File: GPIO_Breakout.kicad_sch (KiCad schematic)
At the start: 3 parts, among them J10 Port C/D breakout, J8 Port A breakout, J9 Port B breakout

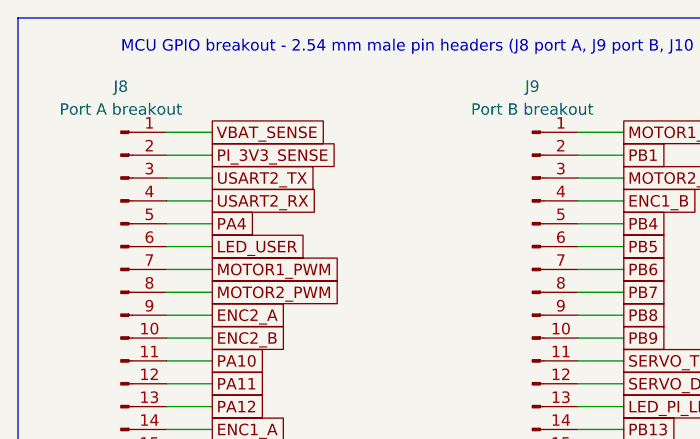
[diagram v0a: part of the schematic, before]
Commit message: Switch AUX ports to top-entry JST XH; drop encoder pull-ups and Pi sense
- J18-J21 (peripheral 5 V ports) are now top-entry JST XH B2B-XH-A:
  cables plug in from above, which suits a flat board you reach into,
  and the footprint drops from 107 to 58 mm2 per port. Use pre-made
  2-pin XH cables, so no crimping.
- Remove the DNP encoder pull-ups R48-R51. If the am-3651 outputs turn
  out to be open-collector, bodge 4.7k from each A/B line to ENCn_5V
  (noted on the Motor Control sheet).
- Remove the Pi-alive sense R44/R45. PA1 is a spare pin again (J8 pin
  2); the Pi's 3V3 on J13 still enables the AUX buck through D15.
- Board: same edits as Update PCB from Schematic (J18-J21 swapped,
  six resistors deleted, PA1 net restored on U1/J8); the parked parts
  are re-grouped beside the board. Venya's tracks unchanged (87).
- Docs, README and schematic PDF updated.

ERC 0/0. DRC: 0 errors, 3 existing text-size warnings, parity clean.
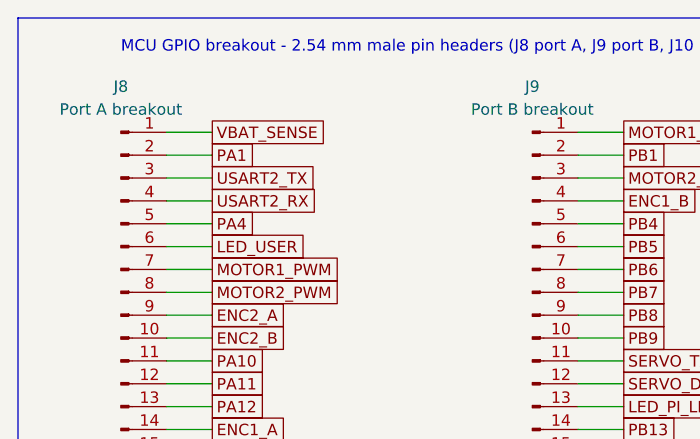
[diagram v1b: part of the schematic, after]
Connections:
- net PI_3V3_SENSE renamed PA1
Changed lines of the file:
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@@
 		)
 	)
-	(global_label "PI_3V3_SENSE"
+	(global_label "PA1"
 		(shape passive)
 		(at 66.04 60.96 0)
@@
 			)
 		)
-		(property "Description" "Male 2.54 mm pin header, 1x15 vertical: pins 1-14 = VBAT_SENSE (PA0), PI_3V3_SENSE (PA1), USART2_TX (PA2), USART2_RX (PA3), PA4, LED_USER (PA5), MOTOR1_PWM (PA6), MOTOR2_PWM (PA7), ENC2_A (PA8), ENC2_B (PA9), PA10, PA11, PA12, ENC1_A (PA15); pin 15 = GND. Every port pin is broken out in port order, including pins already used on the board."
+		(property "Description" "Male 2.54 mm pin header, 1x15 vertical: pins 1-14 = VBAT_SENSE (PA0), PA1, USART2_TX (PA2), USART2_RX (PA3), PA4, LED_USER (PA5), MOTOR1_PWM (PA6), MOTOR2_PWM (PA7), ENC2_A (PA8), ENC2_B (PA9), PA10, PA11, PA12, ENC1_A (PA15); pin 15 = GND. Every port pin is broken out in port order, including pins already used on the board."
 			(at 55.88 76.2 0)
 			(hide yes)

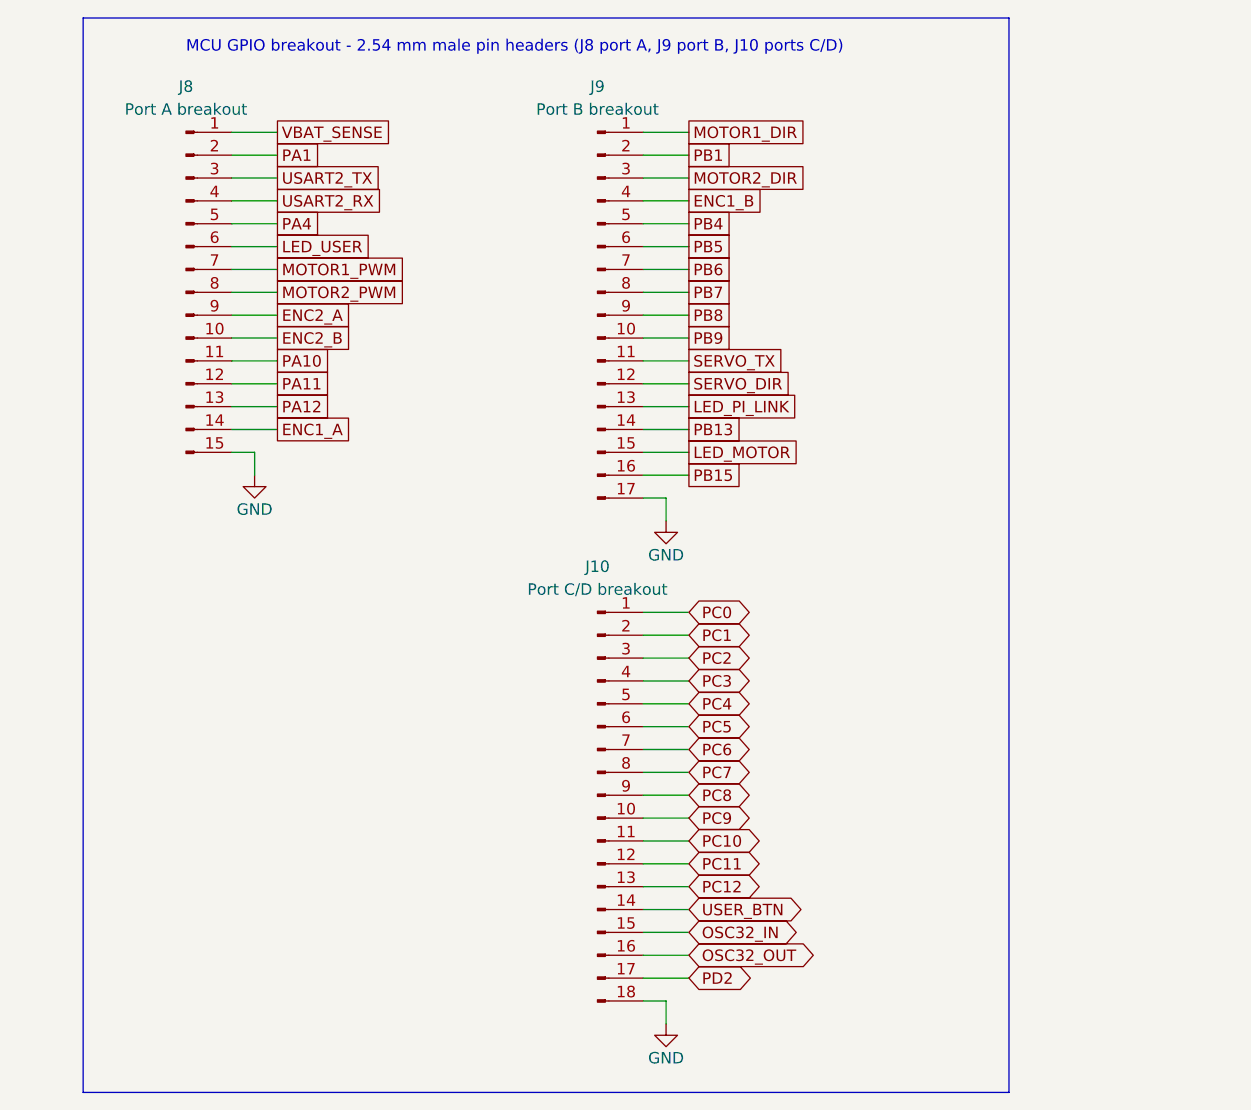
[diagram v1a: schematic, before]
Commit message: Route the board and apply the prototype PCB checklist fixes
Routing
- Route power (pours, In2 power areas, vias) and all signals; add a
  Signal net class (0.15 mm width/clearance) for low-speed nets.
- J8 expansion header is now a 2x8 near the MCU.

Checklist red flags
- Crystal Y3 moved beside U1's OSC pins with C5/C6 outboard and no
  other signals under it.
- Vias untented by default (tented only under silkscreen); 15 mil
  test vias on key signals, recorded as DRC exclusions.
- ESD: U6/U7 split into four USBLC6-2SC6 (U6, U11, U7, U12), one per
  connector, with VBUS caps C50/C51; R12/R13 moved next to J13.
- GND test loop TP3 moved to the top edge beside J5.

Improvements
- Encoder connectors J7/J15 changed to keyed JST XH S4B side-entry.
- 43 passives/LEDs/FB2 moved from 0603 to 0805 (MPNs updated).
- Fifth M3 mounting hole H5 under J8.
- +3.3VA rerouted away from the crystal; acute track angles removed.
- Datasheet links filled in; silkscreen pin labels, pin maps, team
  names and date; reference labels cleared off pads and vias.
- Custom DRC rule for the J7/J15 silkscreen edge overhang.
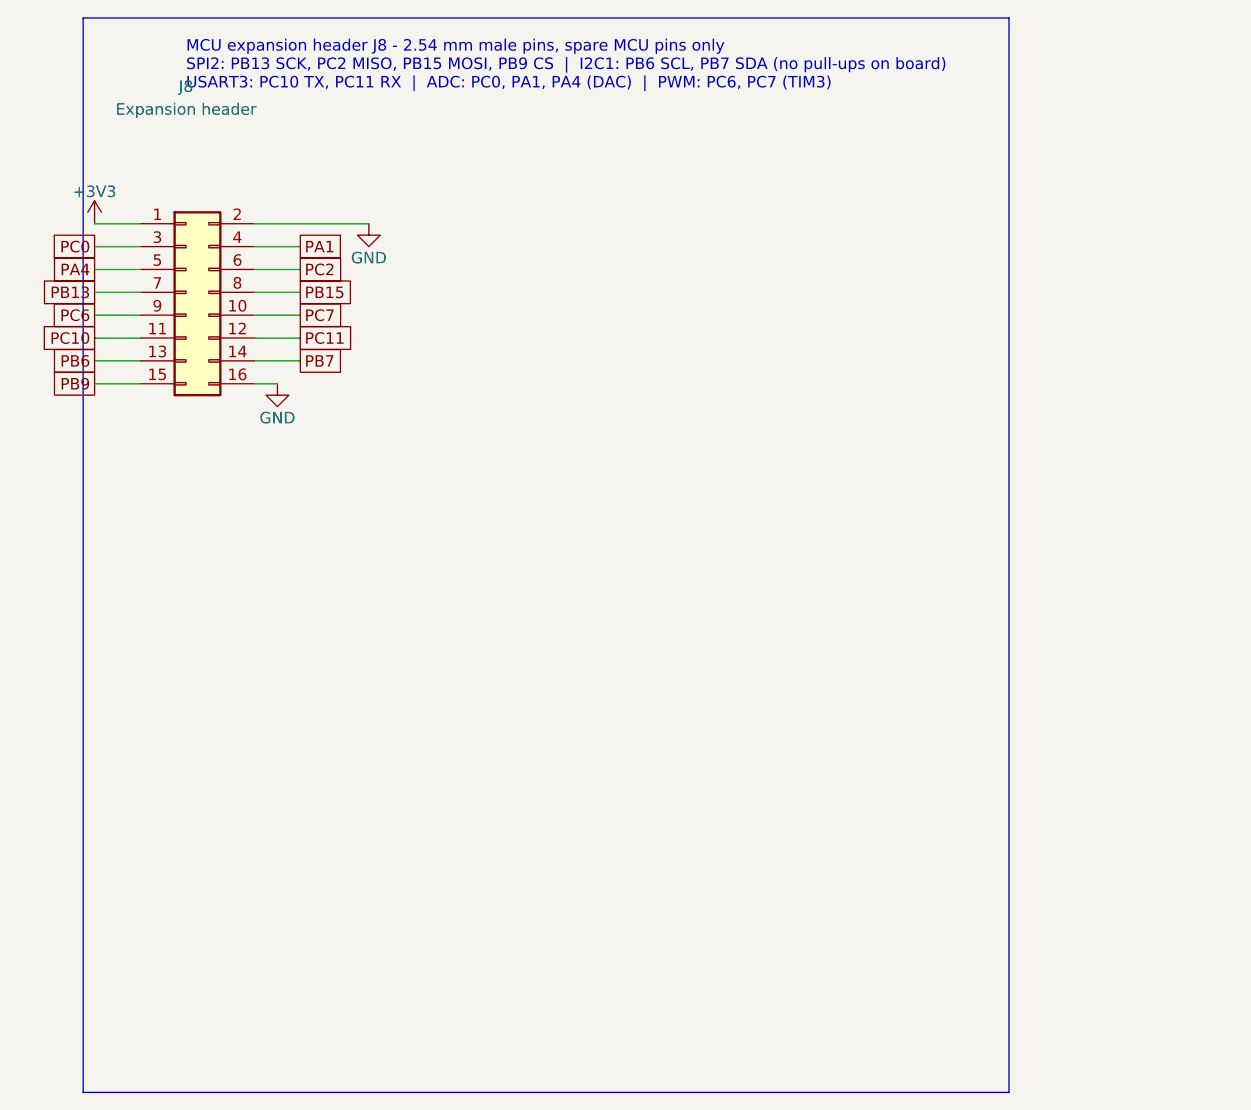
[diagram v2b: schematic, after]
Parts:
- removed J10: Port C/D breakout, Connector_PinHeader_2.54mm:PinHeader_1x18_P2.54mm_Vertical, symbol Connector:Conn_01x18_Pin
- removed J9: Port B breakout, Connector_PinHeader_2.54mm:PinHeader_1x17_P2.54mm_Vertical, symbol Connector:Conn_01x17_Pin
- J8: value Port A breakout -> Expansion header; footprint Connector_PinHeader_2.54mm:PinHeader_1x15_P2.54mm_Vertical -> Connector_PinHeader_2.54mm:PinHeader_2x08_P2.54mm_Vertical; symbol Connector:Conn_01x15_Pin -> Connector_Generic:Conn_02x08_Odd_Even
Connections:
- net ENC1_A is gone; now on net PB7: J8.14 (Pin_14)
- net ENC2_A is gone; now on net PC6: J8.9 (Pin_9)
- net ENC2_B is gone; now on net PC7: J8.10 (Pin_10)
- net LED_USER is gone; now on net PC2: J8.6 (Pin_6)
- net MOTOR1_PWM is gone; now on net PB13: J8.7 (Pin_7)
- net MOTOR2_PWM is gone; now on net PB15: J8.8 (Pin_8)
- net PA10 is gone; now on net PC10: J8.11 (Pin_11)
- net PA11 is gone; now on net PC11: J8.12 (Pin_12)
- net PA12 is gone; now on net PB6: J8.13 (Pin_13)
- net USART2_RX is gone; now on net PA1: J8.4 (Pin_4)
- net USART2_TX is gone; now on net PC0: J8.3 (Pin_3)
- net GND: now also J8.16 (Pin_16), J8.2 (Pin_2); no longer J8.15 (Pin_15)
- net PA1: no longer J8.2 (Pin_2)
- net PB9: now also J8.15 (Pin_15)
- net VBAT_SENSE renamed +3V3
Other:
- note added: "MCU expansion header J8 - 2.54 mm male pins, spare MCU pins only SPI2: PB13 SCK, PC2 MISO, PB15 MOSI, PB9 CS | I2C1: PB6 SCL, PB7 SDA (no pull-ups on board) USART3: PC10 TX, PC11 RX | ADC: PC0, PA1, PA4 (DAC) | PWM: PC6, PC7 (TIM3)"
- note removed: "MCU GPIO breakout - 2.54 mm male pin headers (J8 port A, J9 port B, J10 ports C/D)"
